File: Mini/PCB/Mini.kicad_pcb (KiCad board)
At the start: 2 copper layers, 57 x 38 mm, 0 parts

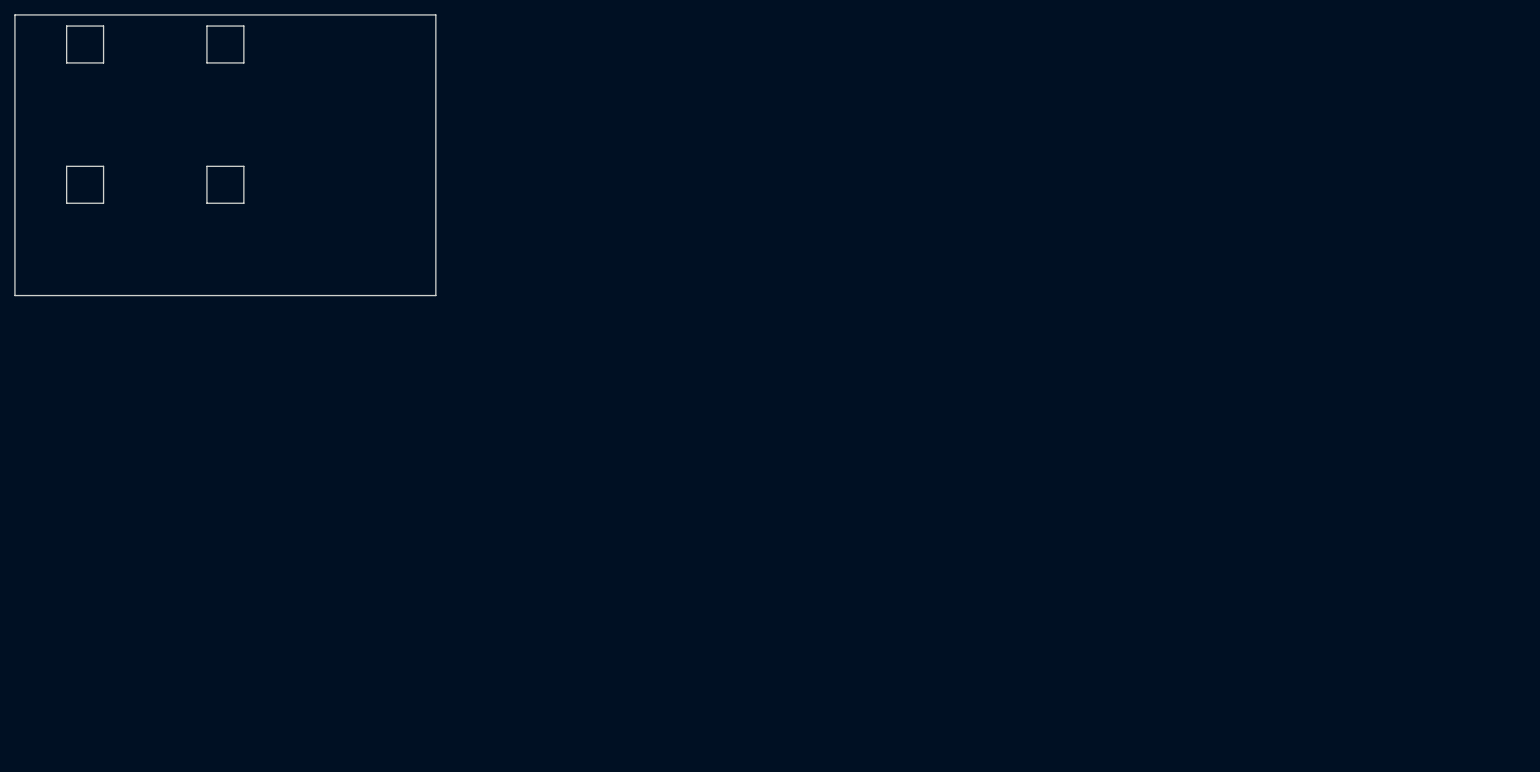
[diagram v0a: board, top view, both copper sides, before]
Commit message: Setting up right hand PCB edge.
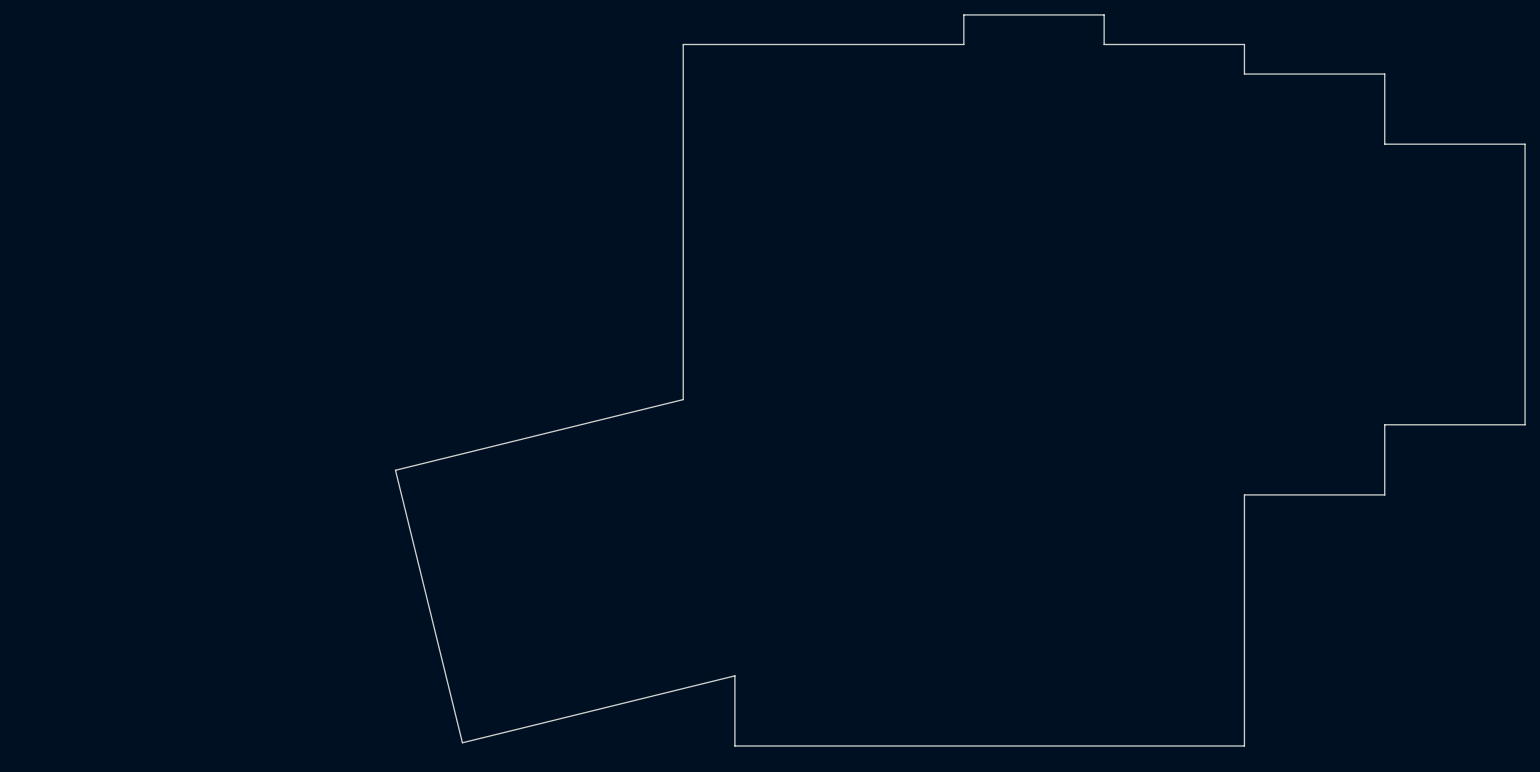
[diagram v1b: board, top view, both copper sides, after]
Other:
- board size 57 x 38 mm -> 153 x 99 mm
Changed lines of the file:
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@@
     (uvia_drill 0.1)
   )
-  (gr_line (start 0 0) (end 57 0) (layer Edge.Cuts) (width 0.05))
-  (gr_line (start 26 25.5) (end 26 20.5) (layer Edge.Cuts) (width 0.05))
-  (gr_line (start 31 25.5) (end 26 25.5) (layer Edge.Cuts) (width 0.05))
-  (gr_line (start 31 20.5) (end 31 25.5) (layer Edge.Cuts) (width 0.05))
-  (gr_line (start 26 20.5) (end 31 20.5) (layer Edge.Cuts) (width 0.05))
-  (gr_line (start 7 25.5) (end 7 20.5) (layer Edge.Cuts) (width 0.05))
-  (gr_line (start 12 25.5) (end 7 25.5) (layer Edge.Cuts) (width 0.05))
-  (gr_line (start 12 20.5) (end 12 25.5) (layer Edge.Cuts) (width 0.05))
-  (gr_line (start 7 20.5) (end 12 20.5) (layer Edge.Cuts) (width 0.05))
-  (gr_line (start 26 6.5) (end 26 1.5) (layer Edge.Cuts) (width 0.05))
-  (gr_line (start 31 6.5) (end 26 6.5) (layer Edge.Cuts) (width 0.05))
-  (gr_line (start 31 1.5) (end 31 6.5) (layer Edge.Cuts) (width 0.05))
-  (gr_line (start 26 1.5) (end 31 1.5) (layer Edge.Cuts) (width 0.05))
-  (gr_line (start 7 6.5) (end 7 1.5) (layer Edge.Cuts) (width 0.05))
-  (gr_line (start 12 6.5) (end 7 6.5) (layer Edge.Cuts) (width 0.05))
-  (gr_line (start 12 1.5) (end 12 6.5) (layer Edge.Cuts) (width 0.05))
-  (gr_line (start 7 1.5) (end 12 1.5) (layer Edge.Cuts) (width 0.05))
-  (gr_line (start 0 38) (end 0 0) (layer Edge.Cuts) (width 0.05))
-  (gr_line (start 57 38) (end 0 38) (layer Edge.Cuts) (width 0.05))
-  (gr_line (start 57 0) (end 57 38) (layer Edge.Cuts) (width 0.05))
+  (gr_line (start 90.5 4) (end 90.5 52.0899) (layer Edge.Cuts) (width 0.05))
+  (gr_line (start 51.533 61.6608) (end 90.5 52.0899) (layer Edge.Cuts) (width 0.05))
+  (gr_line (start 51.533 61.6608) (end 60.597 98.564) (layer Edge.Cuts) (width 0.05))
+  (gr_line (start 60.597 98.564) (end 97.5 89.5) (layer Edge.Cuts) (width 0.05))
+  (gr_line (start 97.5 89.5) (end 97.5 99) (layer Edge.Cuts) (width 0.05))
+  (gr_line (start 97.5 99) (end 166.5 99) (layer Edge.Cuts) (width 0.05))
+  (gr_line (start 166.5 65) (end 166.5 99) (layer Edge.Cuts) (width 0.05))
+  (gr_line (start 166.5 65) (end 185.5 65) (layer Edge.Cuts) (width 0.05))
+  (gr_line (start 185.5 55.5) (end 185.5 65) (layer Edge.Cuts) (width 0.05))
+  (gr_line (start 185.5 55.5) (end 204.5 55.5) (layer Edge.Cuts) (width 0.05))
+  (gr_line (start 204.5 17.5) (end 204.5 55.5) (layer Edge.Cuts) (width 0.05))
+  (gr_line (start 185.5 17.5) (end 204.5 17.5) (layer Edge.Cuts) (width 0.05))
+  (gr_line (start 185.5 8) (end 185.5 17.5) (layer Edge.Cuts) (width 0.05))
+  (gr_line (start 166.5 8) (end 185.5 8) (layer Edge.Cuts) (width 0.05))
+  (gr_line (start 166.5 4) (end 166.5 8) (layer Edge.Cuts) (width 0.05))
+  (gr_line (start 147.5 4) (end 166.5 4) (layer Edge.Cuts) (width 0.05))
+  (gr_line (start 147.5 0) (end 147.5 4) (layer Edge.Cuts) (width 0.05))
+  (gr_line (start 128.5 0) (end 147.5 0) (layer Edge.Cuts) (width 0.05))
+  (gr_line (start 128.5 0) (end 128.5 4) (layer Edge.Cuts) (width 0.05))
+  (gr_line (start 90.5 4) (end 128.5 4) (layer Edge.Cuts) (width 0.05))
 )

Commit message: Laying out pcb.
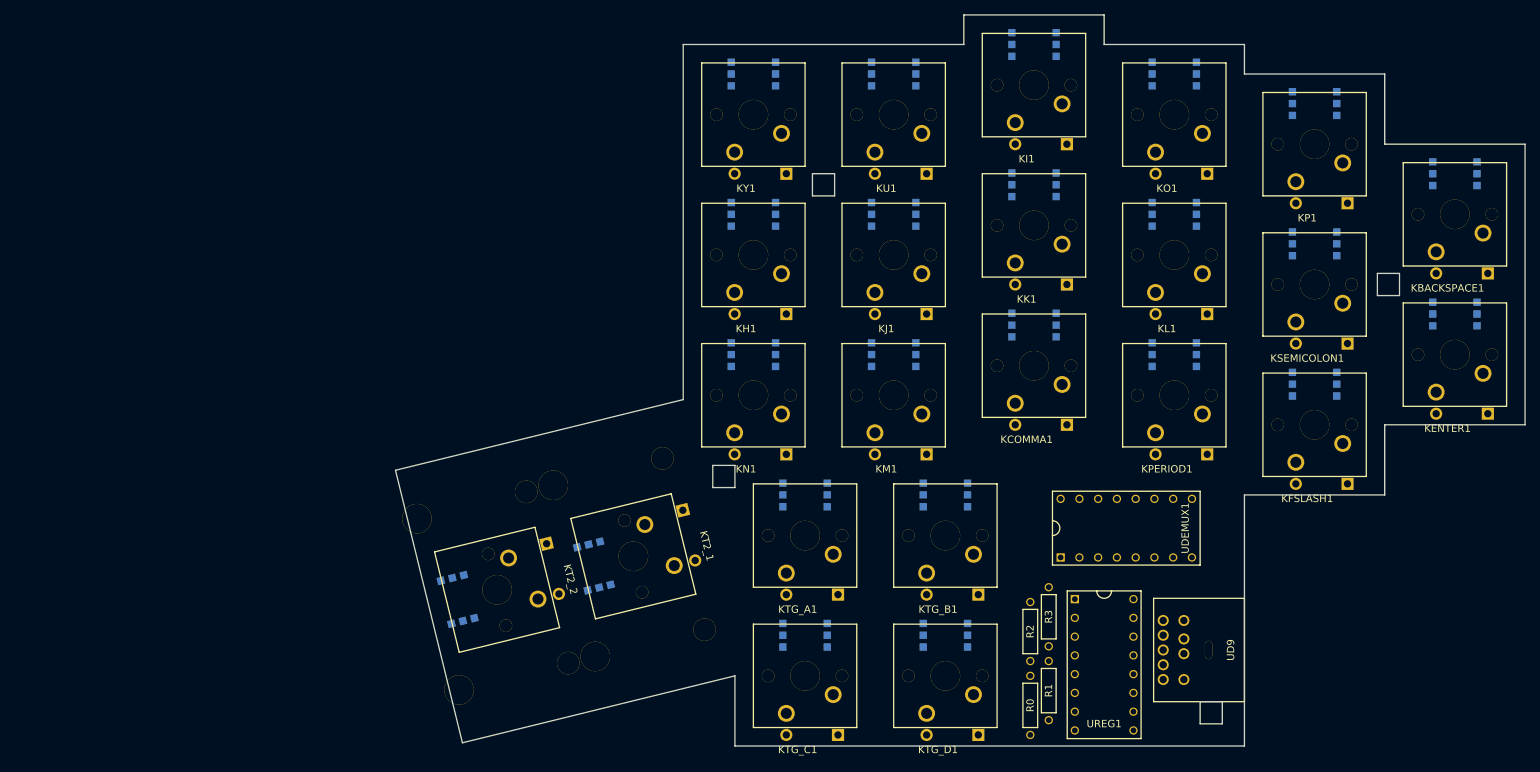
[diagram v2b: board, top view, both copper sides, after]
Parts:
- added KBACKSPACE1: KeyLedDiode, Mini:KeyLedDiodeR2L, F.Cu at (195.0, 27.0)
- added KCOMMA1: KeyLedDiode, Mini:KeyLedDiodeR2L, F.Cu at (138.0, 47.5)
- added KENTER1: KeyLedDiode, Mini:KeyLedDiodeL2R, F.Cu at (195.0, 46.0)
- added KFSLASH1: KeyLedDiode, Mini:KeyLedDiodeR2L, F.Cu at (176.0, 55.5)
- added KH1: KeyLedDiode, Mini:KeyLedDiodeL2R, F.Cu at (100.0, 32.5)
- added KI1: KeyLedDiode, Mini:KeyLedDiodeR2L, F.Cu at (138.0, 9.50)
- added KJ1: KeyLedDiode, Mini:KeyLedDiodeL2R, F.Cu at (119.0, 32.5)
- added KK1: KeyLedDiode, Mini:KeyLedDiodeL2R, F.Cu at (138.0, 28.5)
- added KL1: KeyLedDiode, Mini:KeyLedDiodeL2R, F.Cu at (157.0, 32.5)
- added KM1: KeyLedDiode, Mini:KeyLedDiodeR2L, F.Cu at (119.0, 51.5)
- added KN1: KeyLedDiode, Mini:KeyLedDiodeR2L, F.Cu at (100.0, 51.5)
- added KO1: KeyLedDiode, Mini:KeyLedDiodeR2L, F.Cu at (157.0, 13.5)
- added KP1: KeyLedDiode, Mini:KeyLedDiodeR2L, F.Cu at (176.0, 17.5)
- added KPERIOD1: KeyLedDiode, Mini:KeyLedDiodeR2L, F.Cu at (157.0, 51.5)
- added KSEMICOLON1: KeyLedDiode, Mini:KeyLedDiodeL2R, F.Cu at (176.0, 36.5)
- added KT2_1: KeyLedDiode, Mini:Key2LedDiodeL2R, F.Cu at (83.7, 73.3)
- added KT2_2: KeyLedDiode, Mini:Key2LedDiodeR2L, F.Cu at (65.3, 77.8)
- added KTG_A1: KeyLedDiode, Mini:KeyLedDiodeL2R, F.Cu at (107.0, 70.5)
- added KTG_B1: KeyLedDiode, Mini:KeyLedDiodeL2R, F.Cu at (126.0, 70.5)
- added KTG_C1: KeyLedDiode, Mini:KeyLedDiodeR2L, F.Cu at (107.0, 89.5)
- added KTG_D1: KeyLedDiode, Mini:KeyLedDiodeR2L, F.Cu at (126.0, 89.5)
- added KU1: KeyLedDiode, Mini:KeyLedDiodeR2L, F.Cu at (119.0, 13.5)
- added KY1: KeyLedDiode, Mini:KeyLedDiodeR2L, F.Cu at (100.0, 13.5)
- added R0: R, Mini:PullupResistor, F.Cu at (137.5, 93.5)
- added R1: R, Mini:PullupResistor, F.Cu at (140.0, 91.5)
- added R2: R, Mini:PullupResistor, F.Cu at (137.5, 83.5)
- added R3: R, Mini:PullupResistor, F.Cu at (140.0, 81.5)
- added UD9: MiniDINN9, Mini:MiniDin9, F.Cu at (161.7, 86.0)
- added UDEMUX1: Demultiplexer, Mini:DualInlineMicrochip2x8, F.Cu at (150.5, 69.5)
- added UREG1: ParallelLoadShiftRegister, Mini:DualInlineMicrochip2x8, F.Cu at (147.5, 88.0)
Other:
- outline, holes or cut-outs redrawn

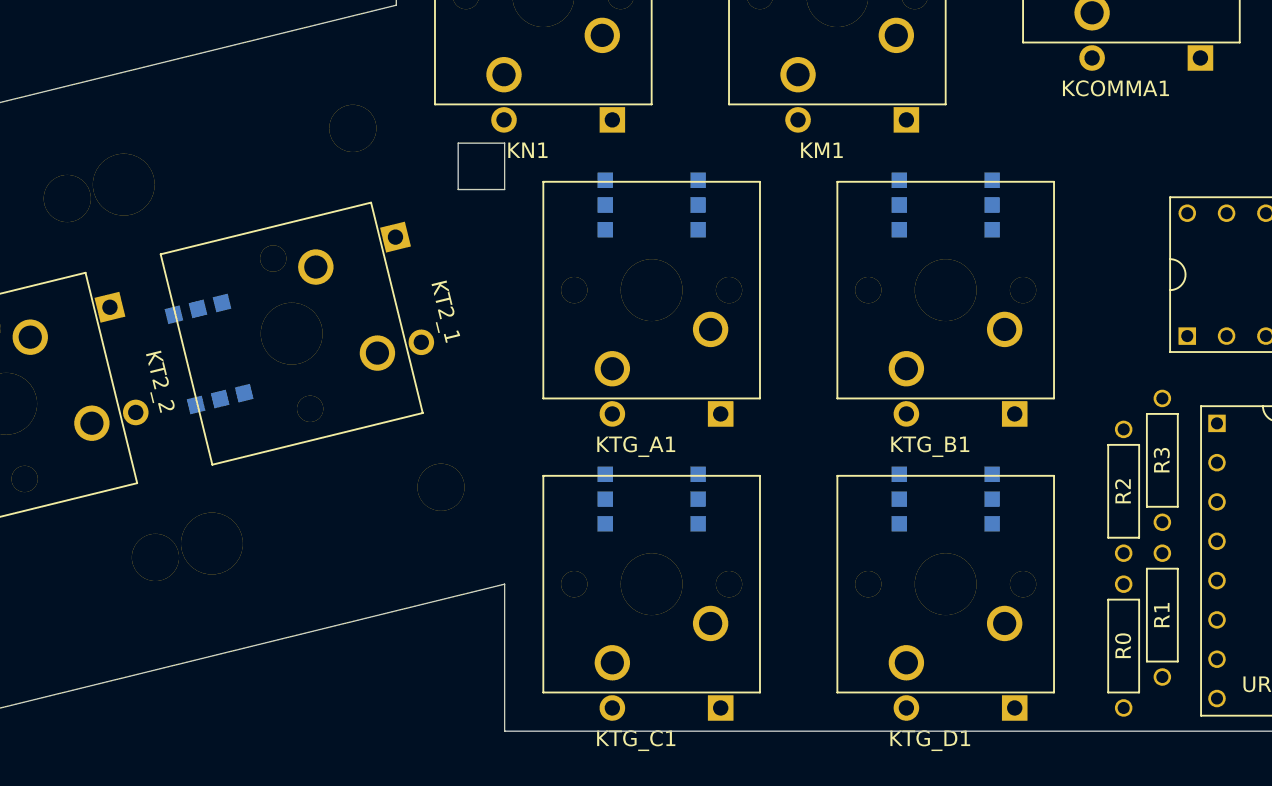
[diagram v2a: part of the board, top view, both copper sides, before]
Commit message: Moving some 2-key holes around.
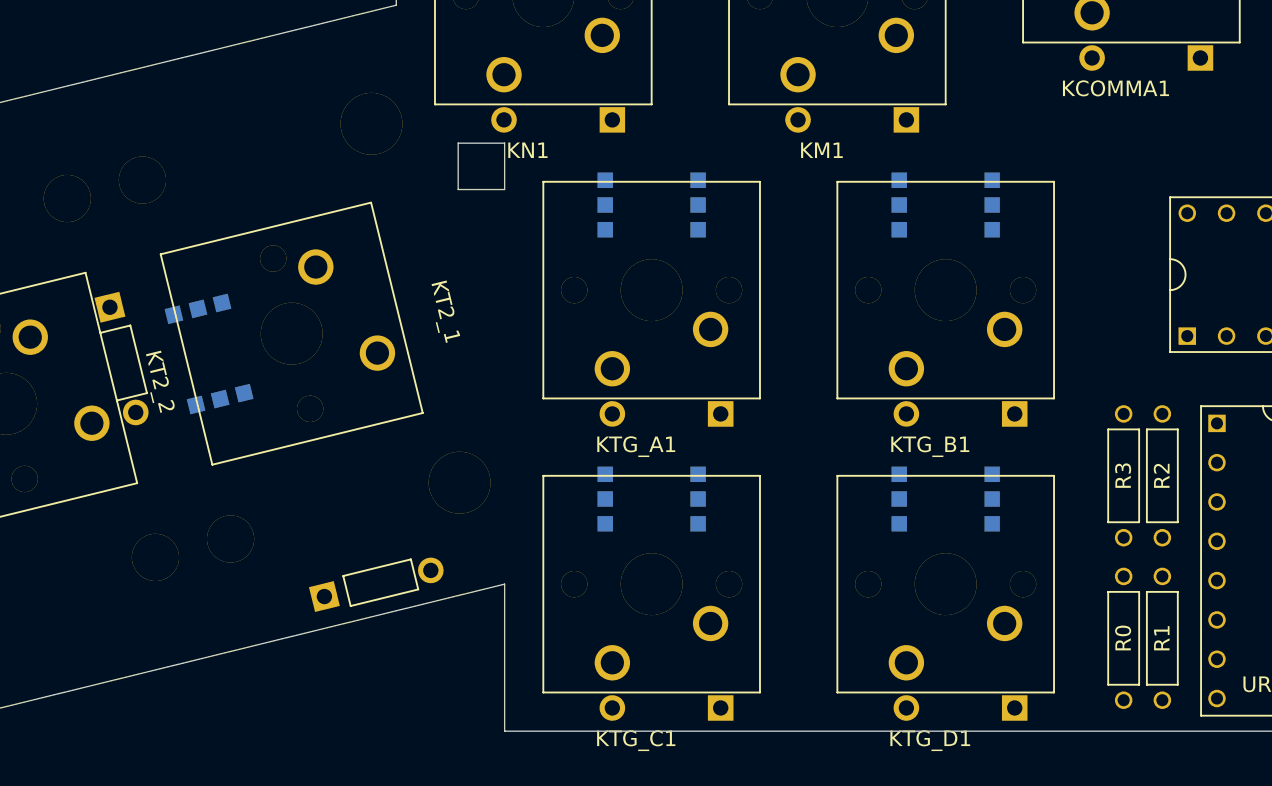
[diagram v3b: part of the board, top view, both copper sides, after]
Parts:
- moved R2 2.69 mm to (140.0, 82.5)
- moved R3 2.69 mm to (137.5, 82.5)
- moved R1 1.50 mm to (140.0, 93.0)
- moved R0 0.50 mm to (137.5, 93.0), turned to 270 degrees

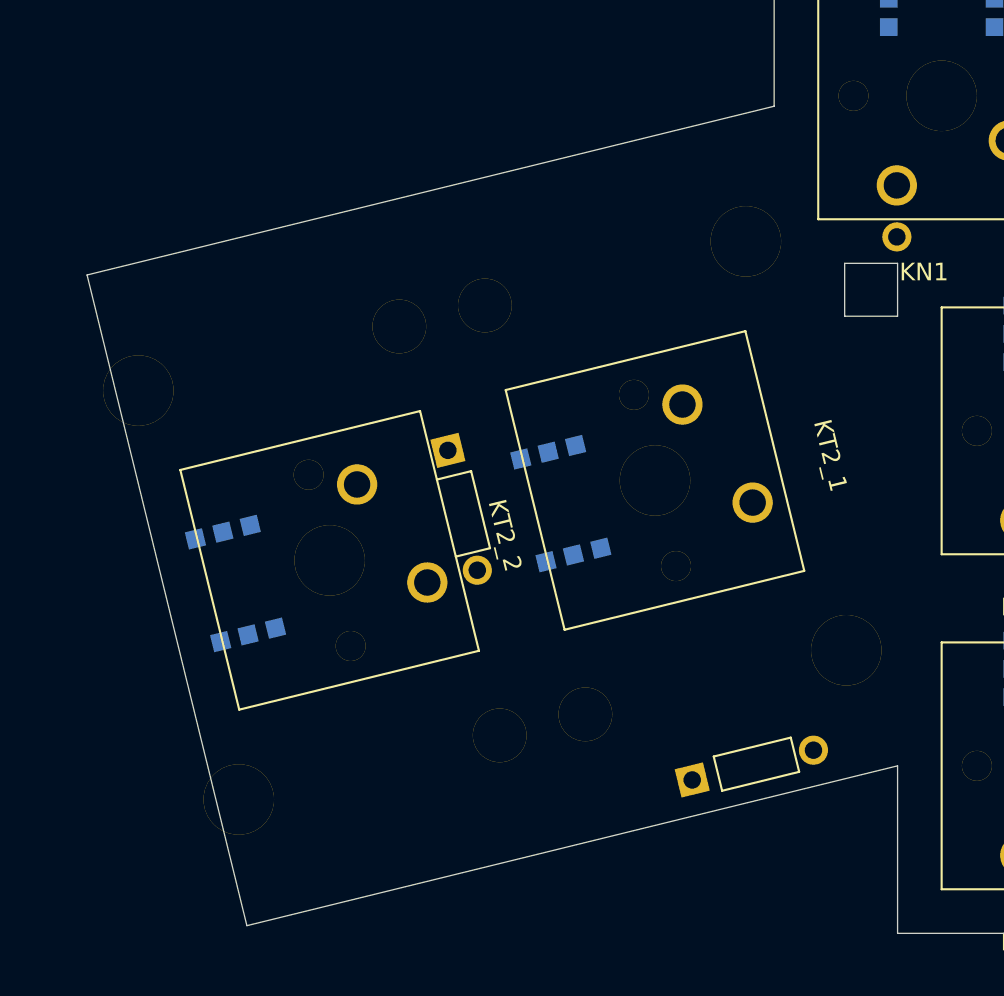
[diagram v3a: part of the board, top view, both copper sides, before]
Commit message: Updating PCB to account for new 3mm thumb 2-key spacing.
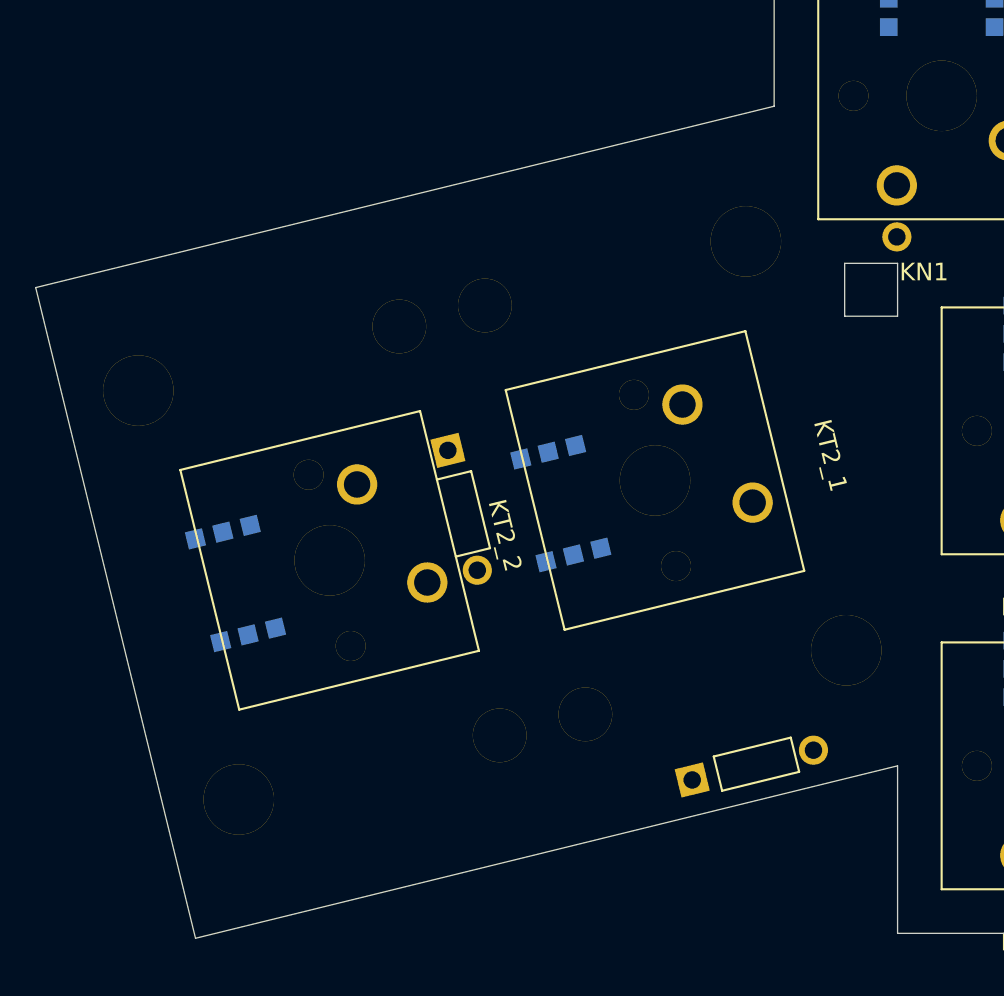
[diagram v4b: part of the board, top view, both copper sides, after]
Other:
- board size 153 x 99 mm -> 155.9 x 99.3 mm
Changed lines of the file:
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@@
   (gr_line (start 163.5 96) (end 163.5 93) (layer Edge.Cuts) (width 0.05))
   (gr_line (start 90.5 4) (end 90.5 52.0899) (layer Edge.Cuts) (width 0.05))
-  (gr_line (start 51.533 61.6608) (end 90.5 52.0899) (layer Edge.Cuts) (width 0.05))
-  (gr_line (start 51.533 61.6608) (end 60.597 98.564) (layer Edge.Cuts) (width 0.05))
-  (gr_line (start 60.597 98.564) (end 97.5 89.5) (layer Edge.Cuts) (width 0.05))
+  (gr_line (start 48.6195 62.3763) (end 90.5 52.0899) (layer Edge.Cuts) (width 0.05))
+  (gr_line (start 48.6195 62.3763) (end 57.6834 99.2795) (layer Edge.Cuts) (width 0.05))
+  (gr_line (start 57.6834 99.2795) (end 97.5 89.5) (layer Edge.Cuts) (width 0.05))
   (gr_line (start 97.5 89.5) (end 97.5 99) (layer Edge.Cuts) (width 0.05))
   (gr_line (start 97.5 99) (end 166.5 99) (layer Edge.Cuts) (width 0.05))
